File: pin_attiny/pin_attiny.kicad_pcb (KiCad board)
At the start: 2 copper layers, 46.6 x 46.6 mm, 27 parts, among them CON1 AVR-ISP-6, SW1 SW_Push, U1 ATTINY85-20SU

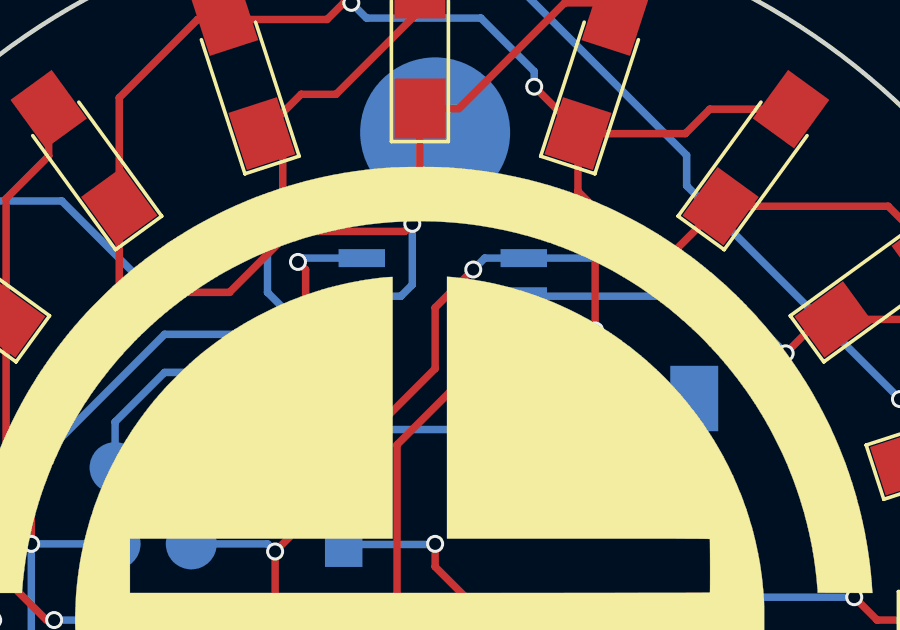
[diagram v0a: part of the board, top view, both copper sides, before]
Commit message: Footprint del attiny cambiado
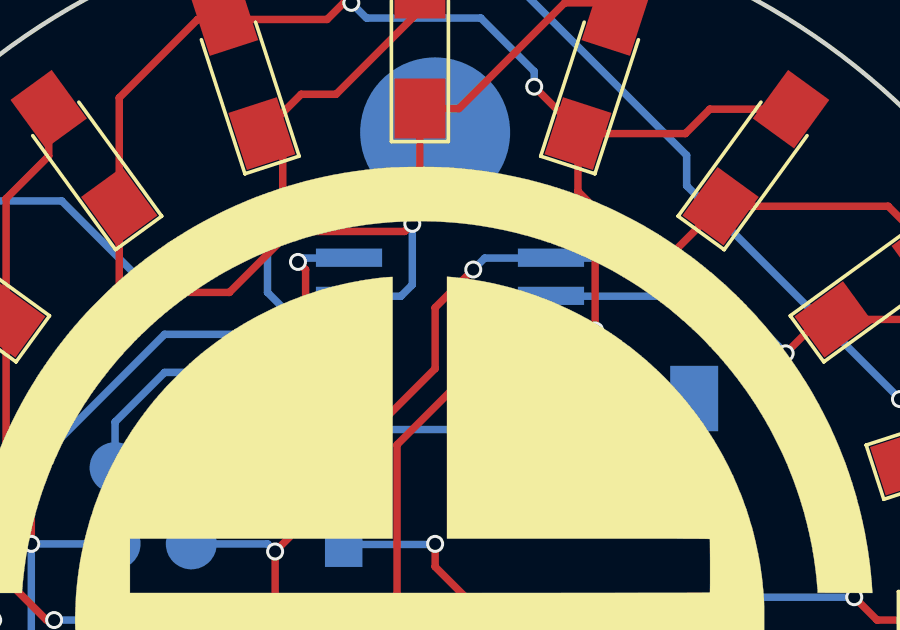
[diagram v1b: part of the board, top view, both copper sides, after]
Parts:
- U1: footprint Housings_SOIC:SOIC-8_3.9x4.9mm_Pitch1.27mm -> SparkFun-DigitalIC:SO08-EIAJ
- moved U1 0.25 mm to (94.0, 87.4), turned to 90 degrees
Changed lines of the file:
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@@
     (area 69.606743 73.924743 116.321257 120.639257)
     (thickness 1.6)
-    (drawings 6)
+    (drawings 7)
     (tracks 290)
     (zones 0)
@@
     (35 F.Paste user)
     (36 B.SilkS user)
-    (37 F.SilkS user)
+    (37 F.SilkS user hide)
     (38 B.Mask user)
     (39 F.Mask user)
@@
     (add_net "Net-(D12-Pad1)")
   )
+  (module SparkFun-DigitalIC:SO08-EIAJ (layer B.Cu)
+    (at 93.98 87.3633 90)
+    (descr "FITS EIAJ PACKAGES (WIDE VERSION OF THE SOIC-8).")
+    (tags "FITS EIAJ PACKAGES (WIDE VERSION OF THE SOIC-8).")
+    (attr smd)
+    (fp_text reference U1 (at -0.254 -0.5588 90) (layer F.SilkS) hide
+      (effects (font (size 0.4064 0.4064) (thickness 0.0254)))
+    )
+    (fp_text value ATTINY85-20SU (at -0.0508 -1.1938 90) (layer F.SilkS) hide
+      (effects (font (size 0.4064 0.4064) (thickness 0.0254)))
+    )
+    (fp_line (start -2.0828 -3.62966) (end -1.7272 -3.62966) (layer Dwgs.User) (width 0.06604))
+    (fp_line (start -1.7272 -3.62966) (end -1.7272 -2.6162) (layer Dwgs.User) (width 0.06604))
+    (fp_line (start -2.0828 -2.6162) (end -1.7272 -2.6162) (layer Dwgs.User) (width 0.06604))
+    (fp_line (start -2.0828 -3.62966) (end -2.0828 -2.6162) (layer Dwgs.User) (width 0.06604))
+    (fp_line (start -0.8128 -3.62966) (end -0.4572 -3.62966) (layer Dwgs.User) (width 0.06604))
+    (fp_line (start -0.4572 -3.62966) (end -0.4572 -2.6162) (layer Dwgs.User) (width 0.06604))
+    (fp_line (start -0.8128 -2.6162) (end -0.4572 -2.6162) (layer Dwgs.User) (width 0.06604))
+    (fp_line (start -0.8128 -3.62966) (end -0.8128 -2.6162) (layer Dwgs.User) (width 0.06604))
+    (fp_line (start 0.4572 -3.62966) (end 0.8128 -3.62966) (layer Dwgs.User) (width 0.06604))
+    (fp_line (start 0.8128 -3.62966) (end 0.8128 -2.6162) (layer Dwgs.User) (width 0.06604))
+    (fp_line (start 0.4572 -2.6162) (end 0.8128 -2.6162) (layer Dwgs.User) (width 0.06604))
+    (fp_line (start 0.4572 -3.62966) (end 0.4572 -2.6162) (layer Dwgs.User) (width 0.06604))
+    (fp_line (start 1.7272 -3.62966) (end 2.0828 -3.62966) (layer Dwgs.User) (width 0.06604))
+    (fp_line (start 2.0828 -3.62966) (end 2.0828 -2.6162) (layer Dwgs.User) (width 0.06604))
+    (fp_line (start 1.7272 -2.6162) (end 2.0828 -2.6162) (layer Dwgs.User) (width 0.06604))
+    (fp_line (start 1.7272 -3.62966) (end 1.7272 -2.6162) (layer Dwgs.User) (width 0.06604))
+    (fp_line (start -2.0828 2.58826) (end -1.7272 2.58826) (layer Dwgs.User) (width 0.06604))
+    (fp_line (start -1.7272 2.58826) (end -1.7272 3.60426) (layer Dwgs.User) (width 0.06604))
+    (fp_line (start -2.0828 3.60426) (end -1.7272 3.60426) (layer Dwgs.User) (width 0.06604))
+    (fp_line (start -2.0828 2.58826) (end -2.0828 3.60426) (layer Dwgs.User) (width 0.06604))
+    (fp_line (start -0.8128 2.58826) (end -0.4572 2.58826) (layer Dwgs.User) (width 0.06604))
+    (fp_line (start -0.4572 2.58826) (end -0.4572 3.60426) (layer Dwgs.User) (width 0.06604))
+    (fp_line (start -0.8128 3.60426) (end -0.4572 3.60426) (layer Dwgs.User) (width 0.06604))
+    (fp_line (start -0.8128 2.58826) (end -0.8128 3.60426) (layer Dwgs.User) (width 0.06604))
+    (fp_line (start 0.4572 2.58826) (end 0.8128 2.58826) (layer Dwgs.User) (width 0.06604))
+    (fp_line (start 0.8128 2.58826) (end 0.8128 3.60426) (layer Dwgs.User) (width 0.06604))
+    (fp_line (start 0.4572 3.60426) (end 0.8128 3.60426) (layer Dwgs.User) (width 0.06604))
+    (fp_line (start 0.4572 2.58826) (end 0.4572 3.60426) (layer Dwgs.User) (width 0.06604))
+    (fp_line (start 1.7272 2.58826) (end 2.0828 2.58826) (layer Dwgs.User) (width 0.06604))
+    (fp_line (start 2.0828 2.58826) (end 2.0828 3.60426) (layer Dwgs.User) (width 0.06604))
+    (fp_line (start 1.7272 3.60426) (end 2.0828 3.60426) (layer Dwgs.User) (width 0.06604))
+    (fp_line (start 1.7272 2.58826) (end 1.7272 3.60426) (layer Dwgs.User) (width 0.06604))
+    (fp_line (start -2.35966 -2.56286) (end 2.35966 -2.56286) (layer Dwgs.User) (width 0.1524))
+    (fp_line (start 2.35966 -2.56286) (end 2.35966 2.53746) (layer Dwgs.User) (width 0.1524))
+    (fp_line (start 2.35966 2.53746) (end -2.35966 2.53746) (layer Dwgs.User) (width 0.1524))
+    (fp_line (start -2.35966 2.53746) (end -2.35966 -2.56286) (layer Dwgs.User) (width 0.1524))
+    (fp_circle (center -2.62636 -2.82448) (end -2.69748 -2.8956) (layer Dwgs.User) (width 0.0635))
+    (pad 1 smd rect (at -1.905 -3.3782 90) (size 0.6096 2.20726) (layers B.Cu B.Paste B.Mask)
+      (net 8 /RESET))
+    (pad 2 smd rect (at -0.635 -3.3782 90) (size 0.6096 2.20726) (layers B.Cu B.Paste B.Mask)
+      (net 3 "Net-(D1-Pad1)"))
+    (pad 3 smd rect (at 0.635 -3.3782 90) (size 0.6096 2.20726) (layers B.Cu B.Paste B.Mask)
+      (net 5 "Net-(D12-Pad1)"))
+    (pad 4 smd rect (at 1.905 -3.3782 90) (size 0.6096 2.20726) (layers B.Cu B.Paste B.Mask)
+      (net 2 GND))
+    (pad 5 smd rect (at 1.905 3.3528 90) (size 0.6096 2.20726) (layers B.Cu B.Paste B.Mask)
+      (net 4 /MOSI))
+    (pad 6 smd rect (at 0.635 3.3528 90) (size 0.6096 2.20726) (layers B.Cu B.Paste B.Mask)
+      (net 6 /MISO))
+    (pad 7 smd rect (at -0.635 3.3528 90) (size 0.6096 2.20726) (layers B.Cu B.Paste B.Mask)
+      (net 7 /SCK))
+    (pad 8 smd rect (at -1.905 3.3528 90) (size 0.6096 2.20726) (layers B.Cu B.Paste B.Mask)
+      (net 1 +3V3))
+  )
   (module Pin_Headers:Pin_Header_Straight_1x01_Pitch2.54mm (layer B.Cu)
     (at 93.472 81.28)
@@
     )
   )
-  (module Housings_SOIC:SOIC-8_3.9x4.9mm_Pitch1.27mm (layer B.Cu)
-    (at 93.726 87.376)
-    (descr "8-Lead Plastic Small Outline (SN) - Narrow, 3.90 mm Body [SOIC] (see Microchip Packaging Specification 00000049BS.pdf)")
-    (tags "SOIC 1.27")
-    (attr smd)
-    (fp_text reference U1 (at 0 3.5) (layer B.SilkS)
-      (effects (font (size 1 1) (thickness 0.15)) (justify mirror))
-    )
-    (fp_text value ATTINY85-20SU (at 0 -3.5) (layer B.Fab)
-      (effects (font (size 1 1) (thickness 0.15)) (justify mirror))
-    )
-    (fp_text user %R (at 0 0) (layer B.Fab)
-      (effects (font (size 1 1) (thickness 0.15)) (justify mirror))
-    )
-    (fp_line (start -0.95 2.45) (end 1.95 2.45) (layer B.Fab) (width 0.1))
-    (fp_line (start 1.95 2.45) (end 1.95 -2.45) (layer B.Fab) (width 0.1))
-    (fp_line (start 1.95 -2.45) (end -1.95 -2.45) (layer B.Fab) (width 0.1))
-    (fp_line (start -1.95 -2.45) (end -1.95 1.45) (layer B.Fab) (width 0.1))
-    (fp_line (start -1.95 1.45) (end -0.95 2.45) (layer B.Fab) (width 0.1))
-    (fp_line (start -3.73 2.7) (end -3.73 -2.7) (layer B.CrtYd) (width 0.05))
-    (fp_line (start 3.73 2.7) (end 3.73 -2.7) (layer B.CrtYd) (width 0.05))
-    (fp_line (start -3.73 2.7) (end 3.73 2.7) (layer B.CrtYd) (width 0.05))
-    (fp_line (start -3.73 -2.7) (end 3.73 -2.7) (layer B.CrtYd) (width 0.05))
-    (fp_line (start -2.075 2.575) (end -2.075 2.525) (layer B.SilkS) (width 0.15))
-    (fp_line (start 2.075 2.575) (end 2.075 2.43) (layer B.SilkS) (width 0.15))
-    (fp_line (start 2.075 -2.575) (end 2.075 -2.43) (layer B.SilkS) (width 0.15))
-    (fp_line (start -2.075 -2.575) (end -2.075 -2.43) (layer B.SilkS) (width 0.15))
-    (fp_line (start -2.075 2.575) (end 2.075 2.575) (layer B.SilkS) (width 0.15))
-    (fp_line (start -2.075 -2.575) (end 2.075 -2.575) (layer B.SilkS) (width 0.15))
-    (fp_line (start -2.075 2.525) (end -3.475 2.525) (layer B.SilkS) (width 0.15))
-    (pad 1 smd rect (at -2.7 1.905) (size 1.55 0.6) (layers B.Cu B.Paste B.Mask)
-      (net 8 /RESET))
-    (pad 2 smd rect (at -2.7 0.635) (size 1.55 0.6) (layers B.Cu B.Paste B.Mask)
-      (net 3 "Net-(D1-Pad1)"))
-    (pad 3 smd rect (at -2.7 -0.635) (size 1.55 0.6) (layers B.Cu B.Paste B.Mask)
-      (net 5 "Net-(D12-Pad1)"))
-    (pad 4 smd rect (at -2.7 -1.905) (size 1.55 0.6) (layers B.Cu B.Paste B.Mask)
-      (net 2 GND))
-    (pad 5 smd rect (at 2.7 -1.905) (size 1.55 0.6) (layers B.Cu B.Paste B.Mask)
-      (net 4 /MOSI))
-    (pad 6 smd rect (at 2.7 -0.635) (size 1.55 0.6) (layers B.Cu B.Paste B.Mask)
-      (net 6 /MISO))
-    (pad 7 smd rect (at 2.7 0.635) (size 1.55 0.6) (layers B.Cu B.Paste B.Mask)
-      (net 7 /SCK))
-    (pad 8 smd rect (at 2.7 1.905) (size 1.55 0.6) (layers B.Cu B.Paste B.Mask)
-      (net 1 +3V3))
-    (model ${KISYS3DMOD}/Housings_SOIC.3dshapes/SOIC-8_3.9x4.9mm_Pitch1.27mm.wrl
-      (at (xyz 0 0 0))
-      (scale (xyz 1 1 1))
-      (rotate (xyz 0 0 0))
-    )
-  )
   (module pin_attiny:logo (layer F.Cu)
     (at 92.964 97.536)
@@
       (xy 7.958667 -12.862278)) (layer F.SilkS) (width 0.01))
   )
+  (gr_line (start 90.7034 90.0938) (end 90.7161 90.0938) (angle 90) (layer B.SilkS) (width 0.2))
   (dimension 29.719085 (width 0.3) (layer Dwgs.User)
     (gr_text 29,719mm (at 93.388821 132.25411 0.4896955931) (layer Dwgs.User)
